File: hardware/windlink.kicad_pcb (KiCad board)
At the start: 2 copper layers, 36 x 26 mm, 27 parts, among them J1 M12A-05PMMR-SF7003, J2 61300411121, SW1 EVP-AWCD4A, SW2 EVP-AWCD4A, U1 AP63203WU-7, U2 PTCAN3413DR, U3 ESP32-C6-MINI-1/U

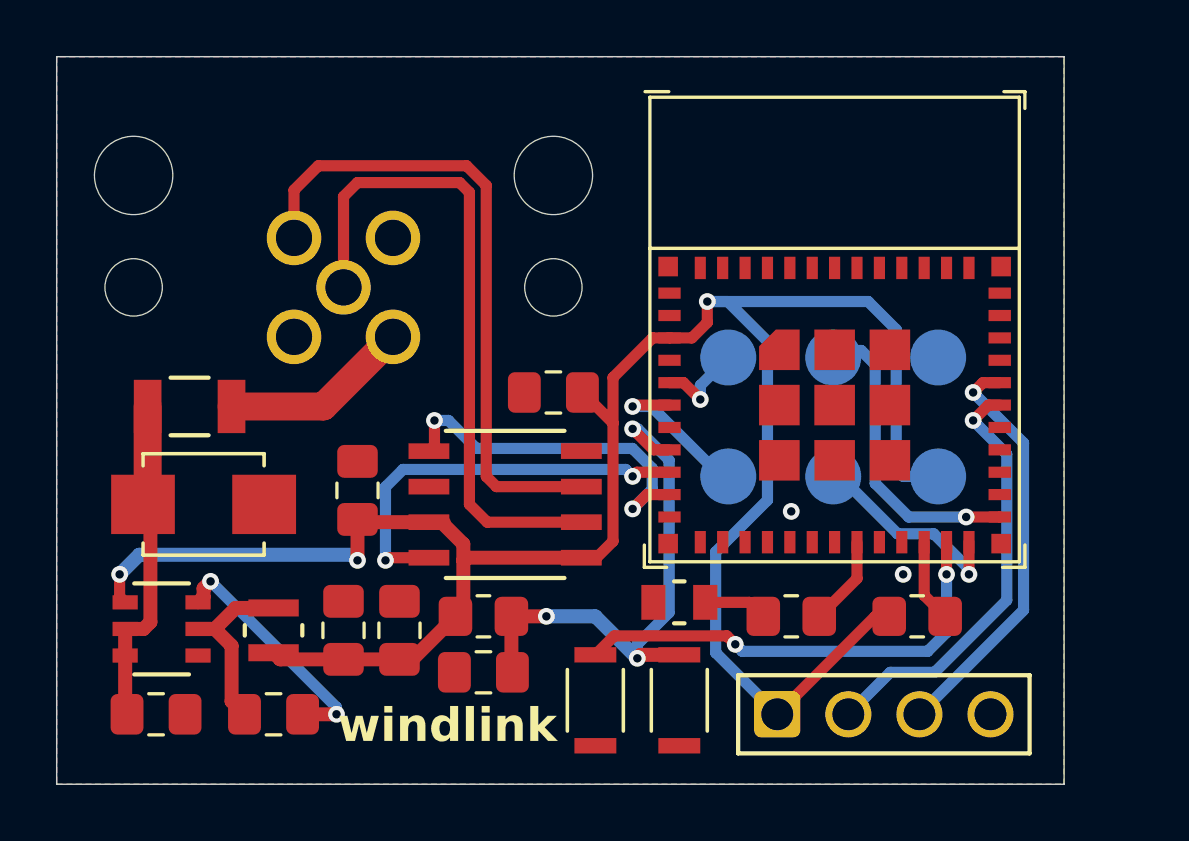
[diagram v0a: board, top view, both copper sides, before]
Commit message: PCB: Add extra flash and antenna cutout
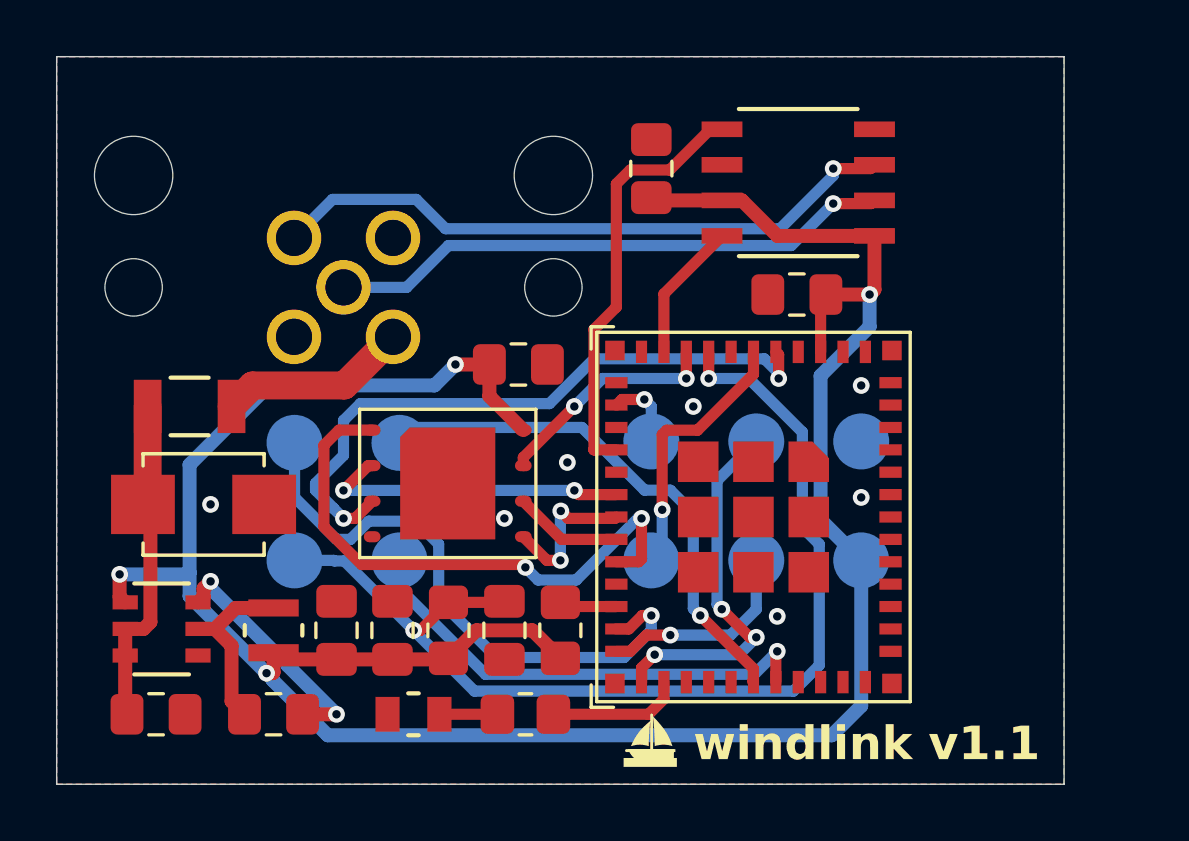
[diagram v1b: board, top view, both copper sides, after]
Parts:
- removed J2: 61300411121, 61300411121:CONN_61300411121_WRE
- removed SW1, SW2: EVP-AWCD4A, EVP_AWCD4A:SW_EVP-AWCD4A
- added C8: 100nf, Capacitor_SMD:C_0805_2012Metric_Pad1.18x1.45mm_HandSolder, F.Cu at (121.2, 87.5)
- added PGM1: TestPoint, TestPoint:TestPoint_Pad_D2.0mm, B.Cu at (113.2, 90.3)
- added RST1: TestPoint, TestPoint:TestPoint_Pad_D2.0mm, B.Cu at (113.2, 94.5)
- added RX1: TestPoint, TestPoint:TestPoint_Pad_D2.0mm, B.Cu at (117.0, 90.3)
- added TX1: TestPoint, TestPoint:TestPoint_Pad_D2.0mm, B.Cu at (117.0, 94.5)
- added U4: BY25FQ64ESWIG(R), BY25FQ64ESWIG(R):BY25FQ64ESWIG(R), F.Cu at (118.7, 91.8)
- moved C5 15.6 mm to (126.0, 80.5)
- moved U2 15.6 mm to (131.2, 81.0)
- moved R3 12.8 mm to (122.8, 97.0), turned to -90 degrees
- moved LED1 10.3 mm to (117.5, 100.0)
- moved R2 10.1 mm to (121.5, 100.0)
- moved C6 9.38 mm to (131.2, 85.0)
- moved U3 6.70 mm to (132.3, 93.0), turned to -90 degrees
- moved GND1 4.07 mm to (133.5, 90.2)
- moved IO1 4.07 mm to (126.0, 90.2)
- moved IO2 4.07 mm to (126.0, 94.5)
- moved IO3 4.07 mm to (129.8, 94.5)
- moved IO4 4.07 mm to (129.8, 90.2)
- moved PWR1 4.07 mm to (133.5, 94.5)
- moved C7 1.68 mm to (120.8, 97.0), turned to -90 degrees
- moved R1 1.35 mm to (118.8, 97.0), turned to 90 degrees
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- renumbered TP6 to GND1, TP1 to IO1, TP2 to IO2, TP3 to IO3, TP4 to IO4, TP5 to PWR1
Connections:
- C7 pad 1: Net-(SW1-A) -> Net-(U3-EN/CHIP_PU)
- IO1 pad 1: Net-(U3-GPIO2/ADC1_CH2) -> Net-(U3-GPIO1/ADC1_CH1/XTAL_32K_N)
- R1 pad 1: Net-(SW1-A) -> 3.3V
- R1 pad 2: 3.3V -> Net-(U3-EN/CHIP_PU)
- R2 pad 1: Net-(U3-GPIO14) -> Net-(U3-GPIO20)
- R3 pad 1: 3.3V -> Net-(U3-GPIO8)
- R3 pad 2: Net-(U3-GPIO8) -> 3.3V
- U3 pad 10: Net-(U2-TXD) -> Net-(U2-RXD)
- U3 pad 13: unconnected-(U3-GPIO1/ADC1_CH1/XTAL_32K_N-Pad13) -> Net-(U3-GPIO1/ADC1_CH1/XTAL_32K_N)
- U3 pad 15: unconnected-(U3-MTCK/GPIO6/ADC1_CH6-Pad15) -> Net-(U2-TXD)
- U3 pad 17: unconnected-(U3-GPIO12/USB_D--Pad17) -> Net-(U3-GPIO12/USB_D-)
- U3 pad 18: unconnected-(U3-GPIO13/USB_D+-Pad18) -> Net-(U3-GPIO13/USB_D+)
- U3 pad 20: unconnected-(U3-GPIO15-Pad20) -> Net-(U3-GPIO15)
- U3 pad 26: unconnected-(U3-GPIO20-Pad26) -> Net-(U3-GPIO20)
- U3 pad 8: Net-(SW1-A) -> Net-(U3-EN/CHIP_PU)
- U3 pad 9: Net-(U2-RXD) -> Net-(U3-MTMS/GPIO4/ADC1_CH4)
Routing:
- net Net-(U3-EN/CHIP_PU): track 0.00 -> 38.6 mm, vias 0 -> 2
- net Net-(U3-GPIO15): track 0.00 -> 20.3 mm, vias 0 -> 2
- net Net-(U3-GPIO2/ADC1_CH2): track 3.26 -> 23.5 mm, vias 1 -> 2
- net Net-(SW1-A): track 19.6 -> 0.00 mm, vias 3 -> 0
- net 3.3V: track 81.0 -> 92.6 mm, vias 3 -> 4
- net Net-(U3-GPIO12/USB_D-): track 0.00 -> 11.2 mm, vias 0 -> 2
- net Net-(U2-RXD): track 14.8 -> 5.00 mm, vias 2 -> 0
- net Net-(U3-MTMS/GPIO4/ADC1_CH4): track 0.00 -> 8.24 mm, vias 0 -> 2
- net Net-(U3-GPIO13/USB_D+): track 0.00 -> 5.56 mm, vias 0 -> 2
- net Net-(U3-GPIO20): track 0.00 -> 4.78 mm
- net Net-(U3-GPIO9): track 16.6 -> 21.1 mm, vias 2 -> 1
- net Net-(U3-GPIO3/ADC1_CH3): track 5.79 -> 9.61 mm
- net Net-(U3-U0RXD/GPIO17): track 15.4 -> 19.0 mm
- net Net-(U2-CANL): track 23.5 -> 20.3 mm, vias 0 -> 1
- net Net-(U3-GPIO1/ADC1_CH1/XTAL_32K_N): track 0.00 -> 2.69 mm, vias 0 -> 1
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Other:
- board text added: "2026 Connor Slade"
- board text added: "windlink v1.1"
- board text added: "↻"
- board text added: "⇌"
- board text added: "⌀"
- board text removed: "2026 Connor Slade windlink v1.0"
- board text removed: "windlink"

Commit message: PCB: Finilize v1.1
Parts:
- moved C8 0.25 mm to (121.5, 87.5)
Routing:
- net GND: vias 7 -> 11
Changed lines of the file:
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@@
 	(footprint "Capacitor_SMD:C_0805_2012Metric_Pad1.18x1.45mm_HandSolder"
 		(layer "F.Cu")
-		(at 121.25 87.5 180)
+		(at 121.5 87.5 180)
 		(descr "Capacitor SMD 0805 (2012 Metric), square (rectangular) end terminal, IPC-7351 nominal with elongated pad for handsoldering. (Body size source: IPC-SM-782 page 76, https://www.pcb-3d.com/wordpress/wp-content/uploads/ipc-sm-782a_amendment_1_and_2.pdf, https://docs.google.com/spreadsheets/d/1BsfQQcO9C6DZCsRaXUlFlo91Tg2WpOkGARC1WS5S8t0/edit?usp=sharing), generated with kicad-footprint-generator")
 		(tags "capacitor handsolder")
@@
 	)
 	(via
+		(at 128.75 85)
+		(size 0.6)
+		(drill 0.3)
+		(layers "F.Cu" "B.Cu")
+		(free yes)
+		(net 1)
+	)
+	(via
 		(at 127.5 89)
+		(size 0.6)
+		(drill 0.3)
+		(layers "F.Cu" "B.Cu")
+		(free yes)
+		(net 1)
+	)
+	(via
+		(at 132.7 97)
+		(size 0.6)
+		(drill 0.3)
+		(layers "F.Cu" "B.Cu")
+		(free yes)
+		(net 1)
+	)
+	(via
+		(at 123.75 97)
+		(size 0.6)
+		(drill 0.3)
+		(layers "F.Cu" "B.Cu")
+		(free yes)
+		(net 1)
+	)
+	(via
+		(at 125.6 85)
 		(size 0.6)
 		(drill 0.3)
@@
 	)
 	(segment
+		(start 120.4625 88.8825)
+		(end 121.425 89.845)
+		(width 0.5)
+		(layer "F.Cu")
+		(net 5)
+	)
+	(segment
 		(start 112.7374 98.0375)
 		(end 112.5 97.8001)
@@
 	)
 	(segment
+		(start 120.4625 87.5)
+		(end 120.4625 88.8825)
+		(width 0.5)
+		(layer "F.Cu")
+		(net 5)
+	)
+	(segment
 		(start 132.05 87.05)
 		(end 132.05 85.1875)
@@
 	)
 	(segment
-		(start 120.2125 87.5)
-		(end 120.2125 88.6325)
-		(width 0.5)
-		(layer "F.Cu")
-		(net 5)
-	)
-	(segment
 		(start 121.75 97)
 		(end 122.75 98)
@@
 		(width 0.5)
 		(layer "F.Cu")
-		(net 5)
-	)
-	(segment
-		(start 120.2125 88.6325)
-		(end 121.425 89.845)
-		(width 0.5)
-		(layer "F.Cu")
